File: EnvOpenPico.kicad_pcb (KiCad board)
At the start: 2 copper layers, 21 x 51.3 mm, 26 parts, among them J1 USB_B_Micro, J2 Conn_01x02, J3 Conn_02x18_Odd_Even, J4 Conn_02x18_Odd_Even, J5 Conn_01x03_Male, U1 NCP1117-3.3_SOT223, U2 W25Q16JVSSIQ, U3 RP2040, Y1 ABLS-12.000MHZ-B4-T

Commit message: Redesign
I need sleep.
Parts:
- removed C8: 1u, Capacitor_SMD:C_0402_1005Metric
- added C10: 1u, Capacitor_SMD:C_0402_1005Metric, F.Cu at (94.1, 60.8)
- added C13: 100n, Capacitor_SMD:C_0402_1005Metric, F.Cu at (95.2, 78.5)
- added C14: 100n, Capacitor_SMD:C_0402_1005Metric, F.Cu at (90.4, 83.6)
- added H1: MountingHole, MountingHole:MountingHole_2.7mm_M2.5, F.Cu at (95.7, 50.4)
- added H2: MountingHole, MountingHole:MountingHole_2.7mm_M2.5, F.Cu at (84.4, 98.3)
- added H3: MountingHole, MountingHole:MountingHole_2.7mm_M2.5, F.Cu at (95.8, 98.3)
- added H4: MountingHole, MountingHole:MountingHole_2.7mm_M2.5, F.Cu at (84.4, 50.4)
- C1: footprint Capacitor_SMD:C_0805_2012Metric -> Capacitor_SMD:C_0402_1005Metric
- C4: footprint Capacitor_SMD:C_0805_2012Metric -> Capacitor_SMD:C_0402_1005Metric; moved to F.Cu
- C5, C7, D2, R1, R2: moved to F.Cu
- U2: footprint W25Q16JVSSIQ:SOIC127P790X216-8N -> Package_SO:SOIC-8_5.23x5.23mm_P1.27mm
- moved C6 12.9 mm to (91.4, 83.7), turned to 270 degrees
- moved C4 8.40 mm to (92.9, 59.5), turned to 180 degrees
- moved C5 7.24 mm to (94.0, 69.0), turned to 0 degrees
- moved D3 5.88 mm to (95.7, 75.4)
- moved R8 5.40 mm to (95.2, 76.9), turned to 180 degrees
- moved R5 5.32 mm to (87.9, 91.3), turned to 180 degrees
- moved R2 4.73 mm to (87.8, 60.4), turned to 270 degrees
- moved C7 4.37 mm to (92.6, 71.4)
- moved R1 4.22 mm to (88.9, 60.4)
- moved J2 4.15 mm to (88.1, 58.5)
- moved U1 3.60 mm to (95.4, 56.6)
- moved C2 2.74 mm to (87.9, 87.6), turned to 0 degrees
- moved C3 2.68 mm to (87.4, 89.3), turned to 90 degrees
- moved U2 2.58 mm to (87.0, 67.0), turned to 270 degrees
- moved C1 1.76 mm to (92.4, 56.3), turned to 270 degrees
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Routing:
- net GND: track 70.5 -> 50.0 mm, vias 10 -> 19
- net /QSPI_SD1: track 6.76 -> 19.3 mm
- net /QSPI_SD3: track 15.5 -> 4.19 mm, vias 2 -> 0
- net /QSPI_SD2: track 7.20 -> 17.4 mm
- net /QSPI_SS: track 13.6 -> 23.7 mm, vias 1 -> 0
- net /QSPI_SCLK: track 15.3 -> 5.16 mm, vias 2 -> 0
- net /QSPI_SD0: track 15.2 -> 6.02 mm, vias 2 -> 0
- net /GPIO25: track 7.35 -> 1.16 mm, vias 2 -> 0
- net +3V3: track 53.2 -> 47.1 mm, vias 3 -> 4
- net /GPIO5: track 14.7 -> 20.7 mm, vias 0 -> 1
- net /XOUT: track 5.72 -> 11.4 mm
- net /RUN: track 9.87 -> 14.6 mm
- net Net-(C3-Pad1): track 8.48 -> 4.05 mm
- net +1V1: track 19.6 -> 15.7 mm, vias 3 -> 5
- net /GPIO4: track 16.8 -> 20.4 mm, vias 0 -> 1
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- added copper zone on F.Cu, net +1V1
- added copper zone on F.Cu, net VBUS
- removed copper zone on B.Cu, net +1V1

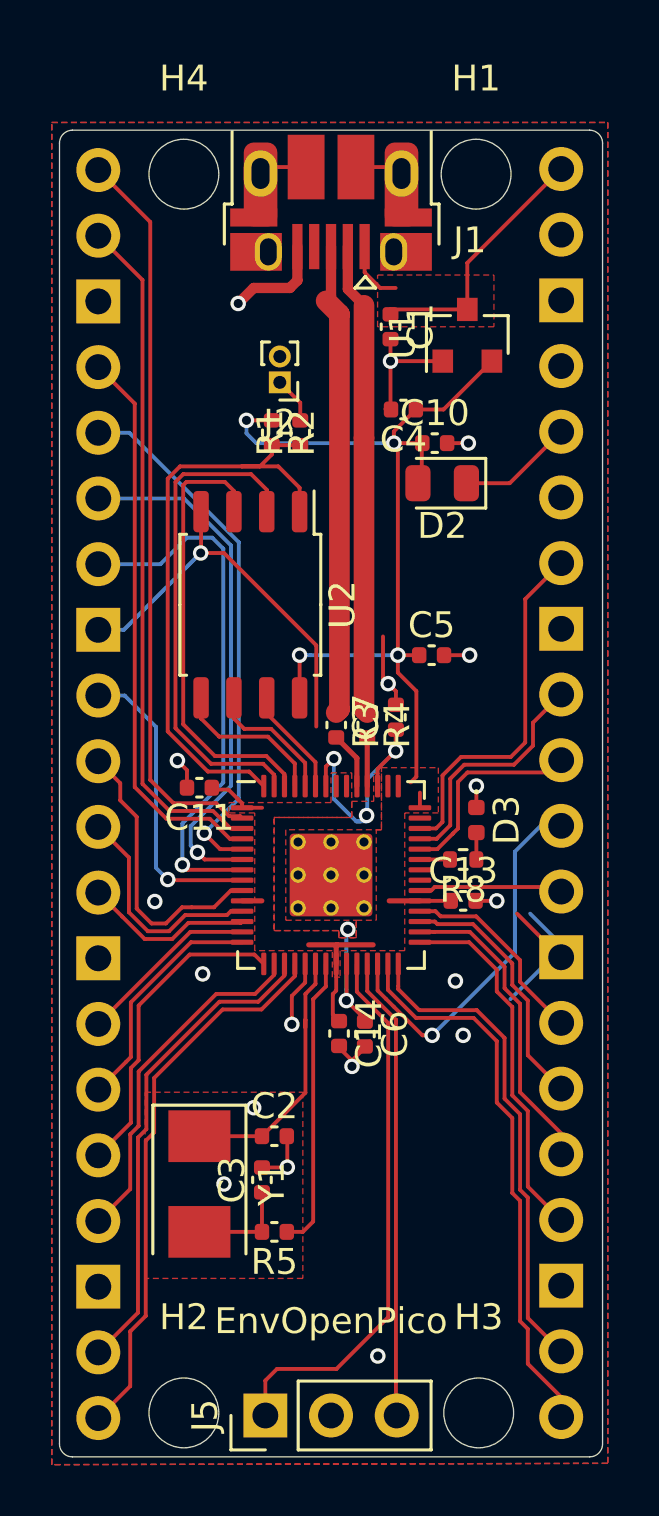
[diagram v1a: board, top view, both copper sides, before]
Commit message: Swapped Crystal for smaller XO oscillator
+ some general other changes
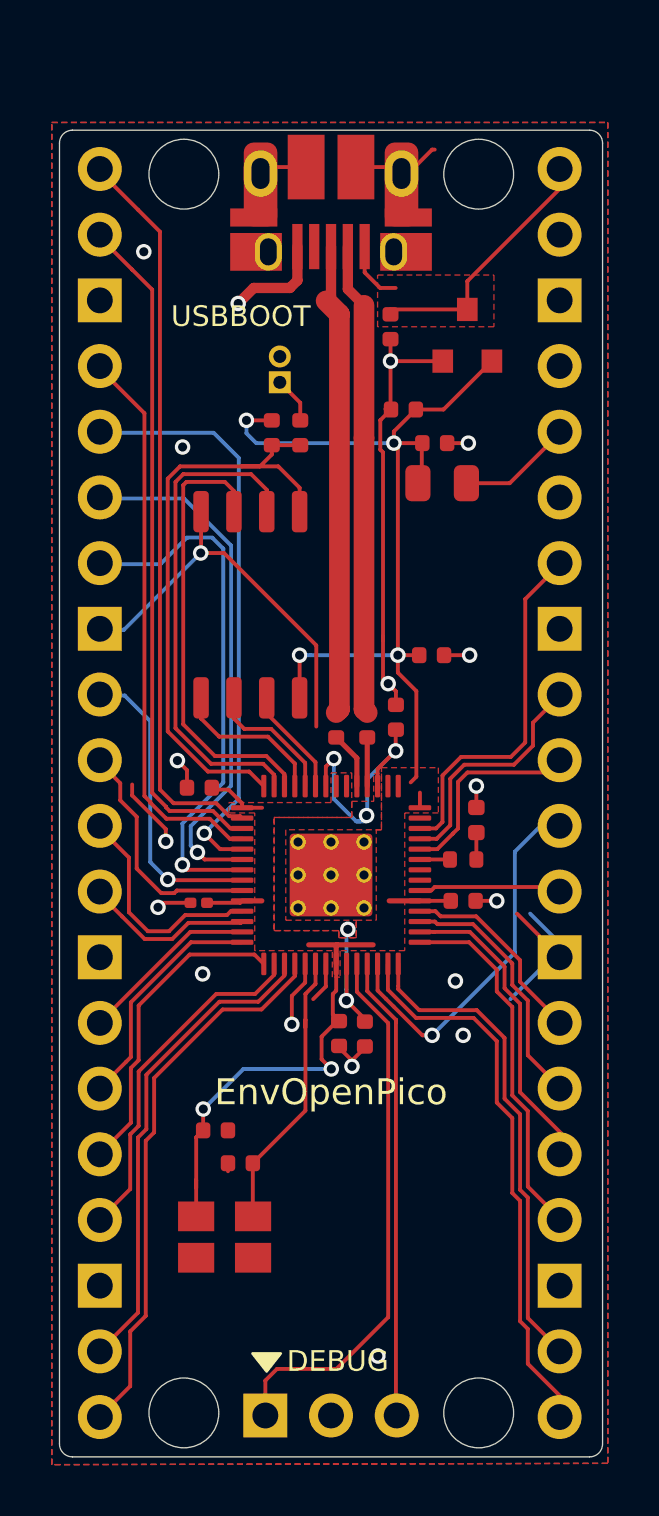
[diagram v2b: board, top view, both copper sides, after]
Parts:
- removed C3: 27p, Capacitor_SMD:C_0402_1005Metric
- removed R5: 1k, Capacitor_SMD:C_0402_1005Metric
- removed Y1: ABLS-12.000MHZ-B4-T, Crystal:Crystal_SMD_5032-2Pin_5.0x3.2mm
- added C15: 100n, Capacitor_SMD:C_0402_1005Metric, F.Cu at (85.6, 87.4)
- added C17: 10u, Capacitor_SMD:C_0201_0603Metric, F.Cu at (85.0, 78.6)
- added X1: XO32, Crystal:Crystal_SMD_SeikoEpson_TSX3225-4Pin_3.2x2.5mm, F.Cu at (86.0, 91.5)
- C2: value 27p -> 15p
- moved C2 1.68 mm to (86.6, 88.6)
- moved H1 0.10 mm to (95.8, 50.4)
- moved J3 0.07 mm to (81.2, 98.5)
- moved J4 0.06 mm to (98.9, 50.2)
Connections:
- C2 pad 1: /XIN -> GND
- C2 pad 2: GND -> /XIN
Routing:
- net +3V3: track 47.1 -> 60.9 mm, vias 4 -> 6
- net GND: track 50.0 -> 62.9 mm
- net /XOUT: track 11.4 -> 1.57 mm
- net Net-(C3-Pad1): track 4.05 -> 0.00 mm
- net /GPIO3: track 20.7 -> 22.6 mm
- net /GPIO7: track 11.2 -> 9.28 mm
- net /XIN: track 10.3 -> 11.1 mm
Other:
- board text added: "3.3V_EN is not implemented"
- board text added: "ADC_VREF is not implemented"
- board text added: "DEBUG"
- board text added: "USBBOOT"
- board text added: "VSYS is not implemented"

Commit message: added more decoupling capacitors+++others
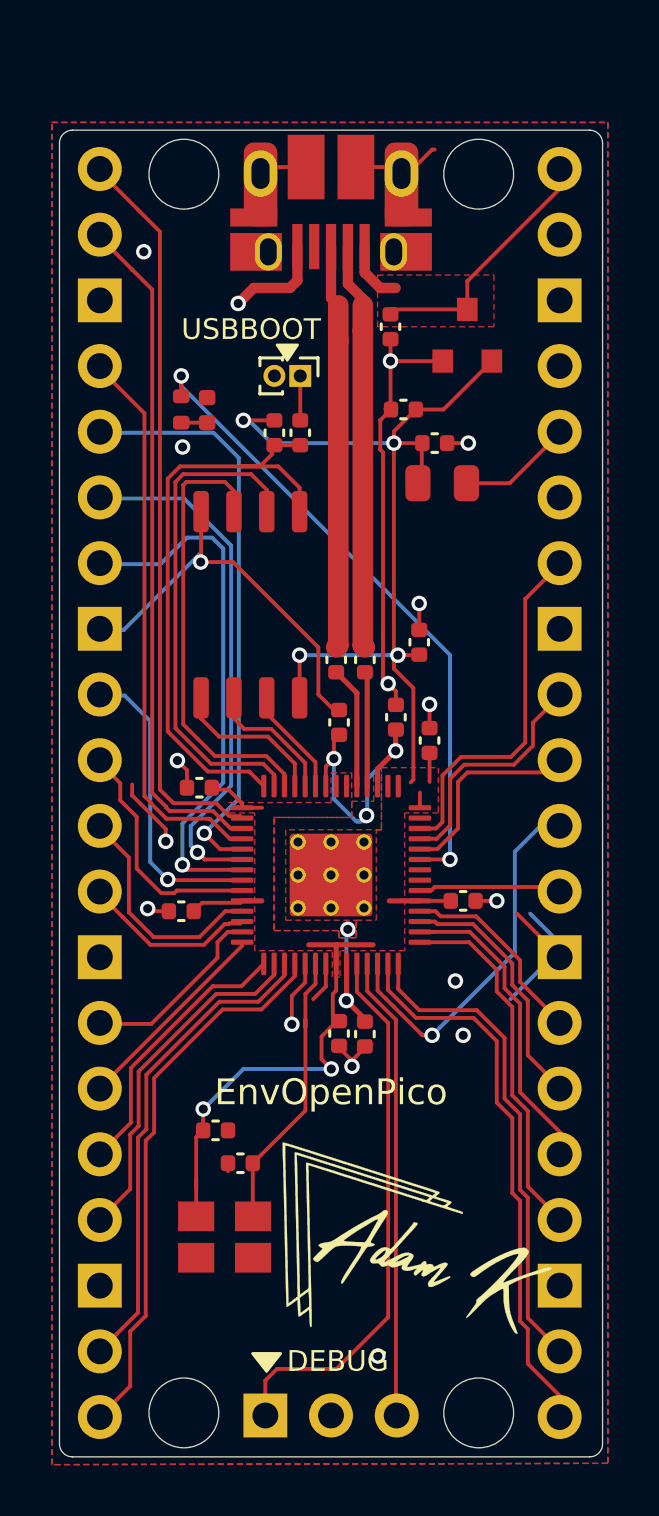
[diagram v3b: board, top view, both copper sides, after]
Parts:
- added C3: 1u, Capacitor_SMD:C_0402_1005Metric, F.Cu at (90.4, 71.6)
- added C8: 100n, Capacitor_SMD:C_0402_1005Metric, F.Cu at (93.9, 72.3)
- added G***: LOGO, EnvExtras:logo, F.Cu at (93.5, 91.7)
- C17: footprint Capacitor_SMD:C_0201_0603Metric -> Capacitor_SMD:C_0402_1005Metric
- moved R8 20.5 mm to (84.3, 59.5), turned to 90 degrees
- moved D3 19.0 mm to (85.3, 59.5)
- moved R4 2.52 mm to (91.4, 69.2)
- moved R3 2.52 mm to (90.3, 69.2)
- moved J2 0.83 mm to (88.9, 58.2), turned to 270 degrees
- moved C17 0.75 mm to (84.3, 78.9)
- moved C5 0.69 mm to (93.5, 68.5), turned to 90 degrees
- moved R2 0.10 mm to (87.9, 60.4)
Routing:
- net /GPIO25: track 1.16 -> 25.0 mm, vias 0 -> 2
- net /USB_D+: track 18.4 -> 15.6 mm
- net Net-(R4-Pad2): track 1.88 -> 4.44 mm
- net /USB_D-: track 18.3 -> 15.8 mm
- net Net-(R3-Pad2): track 2.21 -> 4.73 mm
- net +3V3: track 60.9 -> 62.7 mm
- net /GPIO12: track 12.2 -> 10.7 mm
- net /GPIO11: track 9.16 -> 8.00 mm
- net +1V1: track 15.7 -> 16.7 mm
- net GND: track 62.9 -> 62.4 mm, vias 19 -> 18

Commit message: Replaced MicroB with Type-C
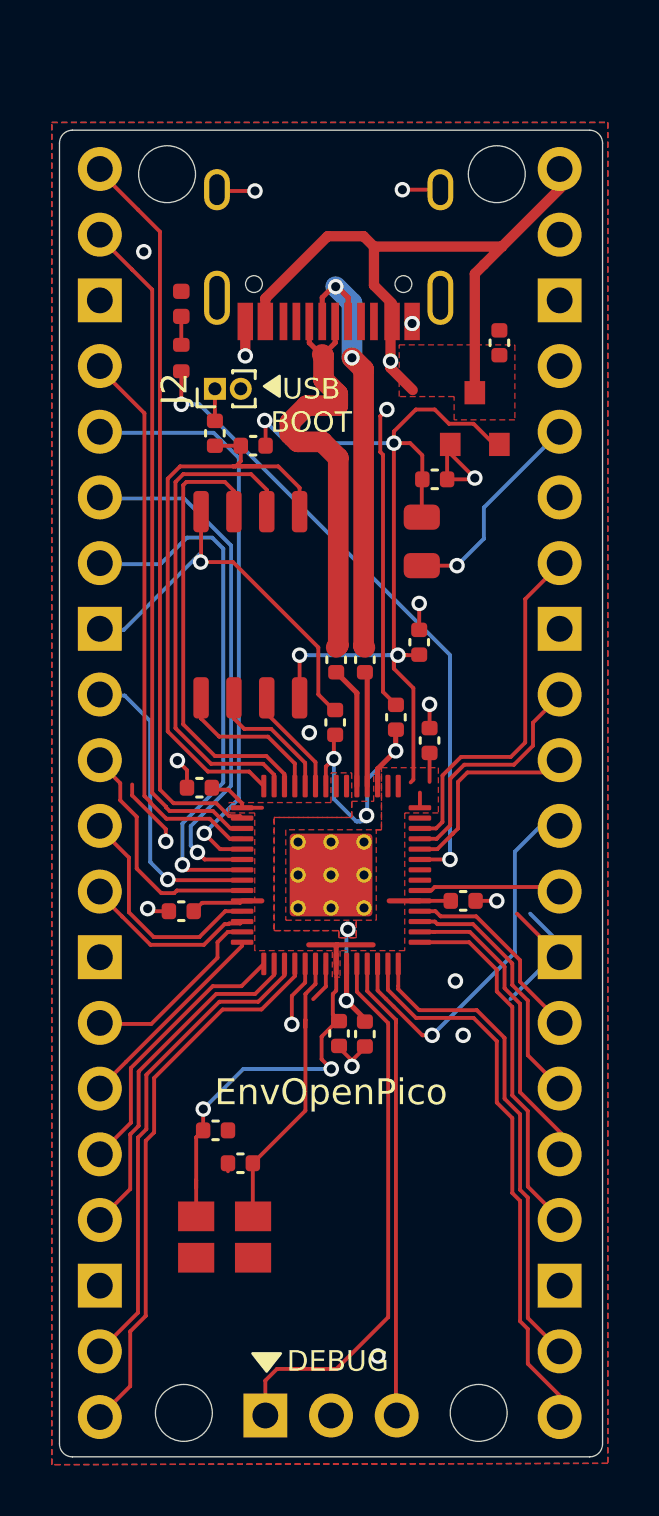
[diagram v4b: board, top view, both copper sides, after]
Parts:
- removed C4: 10u, Capacitor_SMD:C_0402_1005Metric
- removed G***: LOGO, EnvExtras:logo
- removed J1: USB_B_Micro, RP2040_minimal:USB_Micro-B_Amphenol_10103594-0001LF_Horizontal_modified
- added e1: USB_C, HRO-TYPE-C31-M-12:HRO-TYPE-C-31-M-12, F.Cu at (90.0, 48.4)
- H1, H2, H3, H4: footprint MountingHole:MountingHole_2.7mm_M2.5 -> MountingHole:MountingHole_2.2mm_M2
- moved C1 4.26 mm to (96.6, 56.9), turned to 90 degrees
- moved D3 4.23 mm to (84.3, 55.4)
- moved J2 3.34 mm to (85.6, 58.7), turned to 90 degrees
- moved R1 3.30 mm to (85.6, 60.4)
- moved U1 3.23 mm to (95.7, 59.9)
- moved D2 2.38 mm to (93.6, 64.6), turned to 90 degrees
- moved R8 1.99 mm to (84.3, 57.5), turned to 270 degrees
- moved C10 1.40 mm to (94.1, 62.2)
- moved R2 0.96 mm to (87.1, 60.9), turned to 180 degrees
- moved H1 0.70 mm to (96.5, 50.4)
- moved H4 0.65 mm to (83.8, 50.4)
- moved C3 0.15 mm to (90.2, 71.6)
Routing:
- net VBUS: track 12.6 -> 27.2 mm, vias 0 -> 1
- net GND: track 62.4 -> 55.5 mm, vias 18 -> 20
- net Net-(D2-Pad1): track 4.49 -> 8.18 mm, vias 0 -> 1
- net /USB_D-: track 15.8 -> 17.6 mm, vias 0 -> 2
- net /USB_D+: track 15.6 -> 17.3 mm
- net +3V3: track 62.7 -> 63.3 mm
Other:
- board text added: "USB BOOT"
- board text removed: "USBBOOT"

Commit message: I forgot what I went to adjust but I did something or another.
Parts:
- moved C5 2.63 mm to (96.1, 68.9), turned to 180 degrees
- moved R3 2.60 mm to (91.7, 71.4)
- moved R4 2.54 mm to (92.6, 71.4)
- moved C8 2.35 mm to (96.0, 73.3)
- moved D2 2.25 mm to (95.7, 63.7), turned to 0 degrees
- moved C10 2.03 mm to (96.1, 62.1), turned to 180 degrees
- moved C7 1.80 mm to (94.1, 72.3)
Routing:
- net GND: track 55.5 -> 39.1 mm, vias 20 -> 19
- net /USB_D+: track 17.3 -> 20.8 mm, vias 0 -> 1
- net /USB_D-: track 17.6 -> 20.3 mm
- net Net-(R3-Pad2): track 4.73 -> 2.41 mm
- net +1V1: track 16.7 -> 18.4 mm
- net Net-(R4-Pad2): track 4.44 -> 3.06 mm
- net /GPIO25: track 24.8 -> 26.0 mm
- net /GPIO26_ADC0: track 7.94 -> 6.83 mm
- net +3V3: track 63.3 -> 64.4 mm

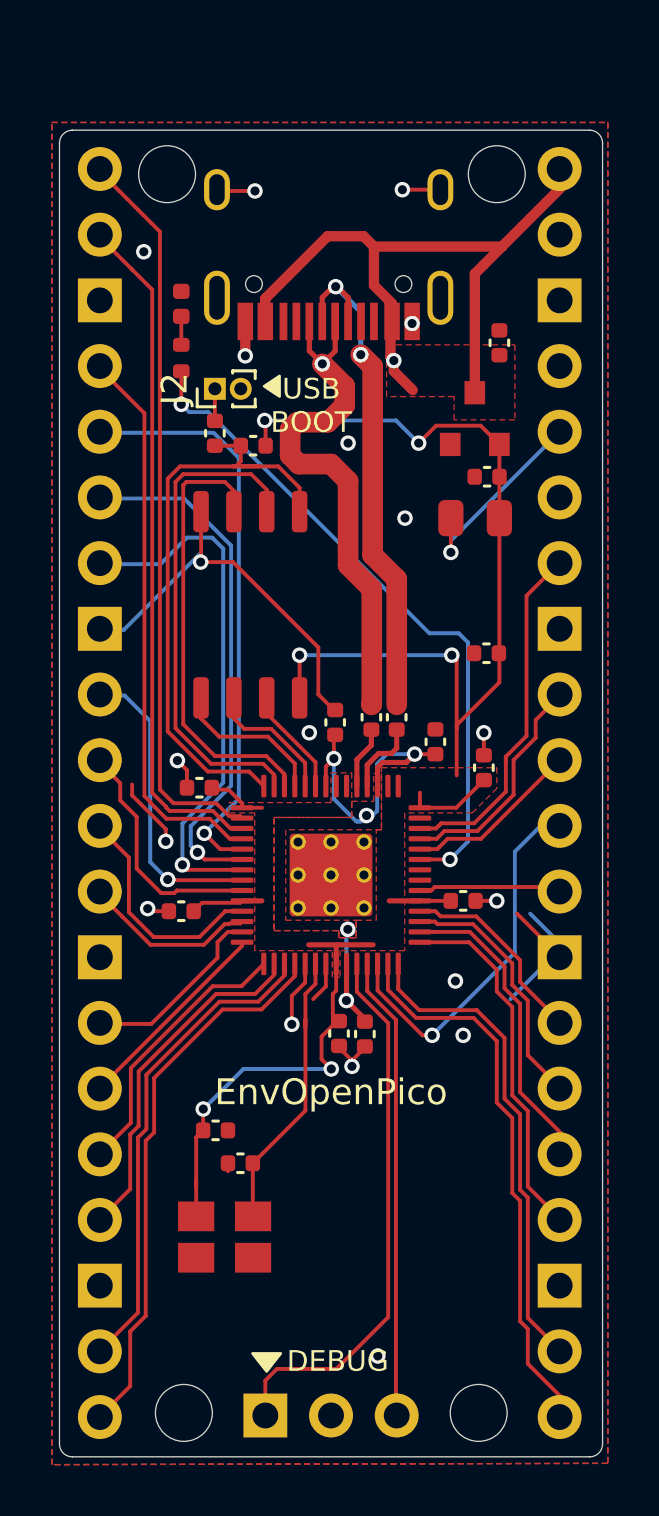
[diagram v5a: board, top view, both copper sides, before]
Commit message: replaced the 3.3V out diode for a smaller one
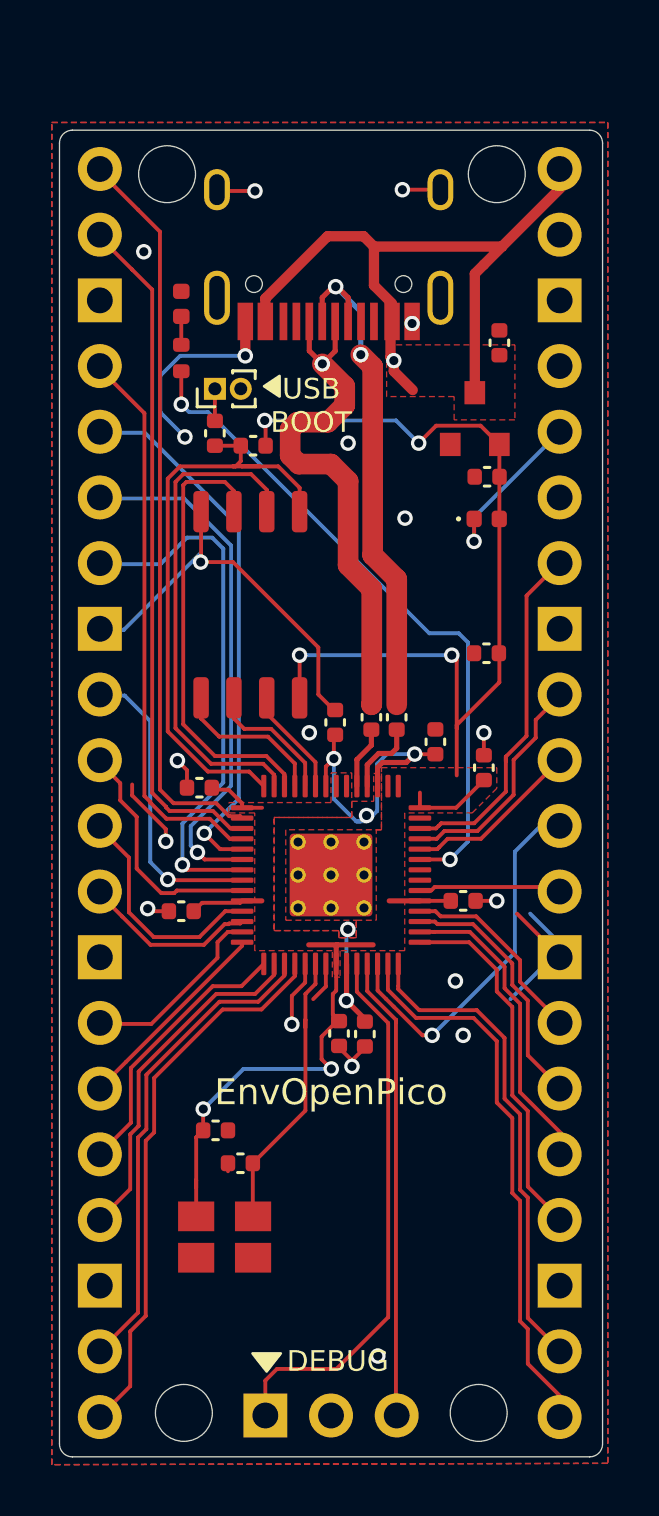
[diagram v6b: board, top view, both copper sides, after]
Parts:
- D2: footprint Diode_SMD:D_0805_2012Metric -> Diode_SMD:D_0402_1005Metric
- moved D2 0.45 mm to (96.1, 63.7)
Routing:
- net GND: track 39.1 -> 45.4 mm, vias 19 -> 20
- net /GPIO3: track 22.6 -> 21.1 mm
- net Net-(D2-Pad1): track 7.73 -> 6.48 mm

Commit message: Made the board 0.09mm wider and adjusted the ground planes
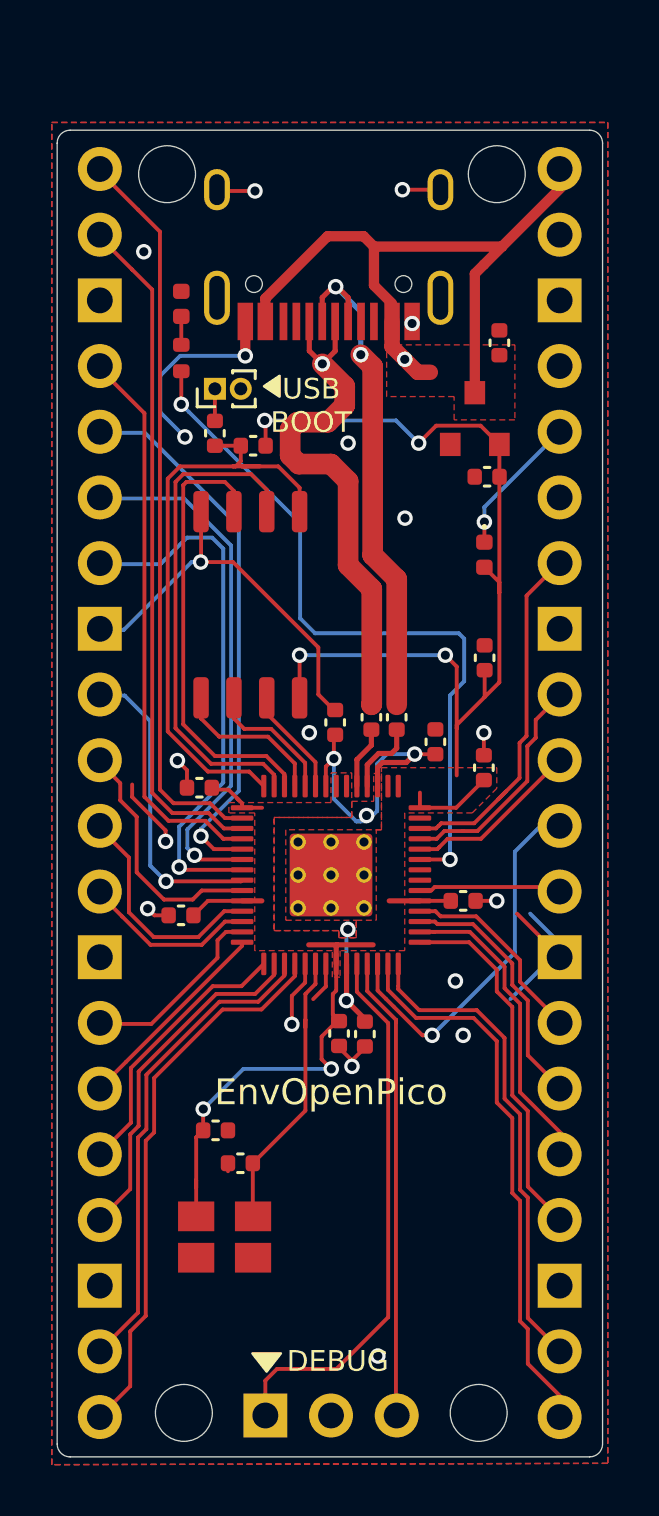
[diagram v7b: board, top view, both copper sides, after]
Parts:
- moved D2 1.39 mm to (96.0, 65.1), turned to 270 degrees
- moved C5 0.19 mm to (96.0, 69.1), turned to 90 degrees
- moved C17 0.16 mm to (84.3, 79.1)
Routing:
- net +3V3: track 64.4 -> 66.5 mm
- net /GPIO25: track 26.0 -> 28.1 mm
- net Net-(D2-Pad1): track 6.48 -> 5.48 mm
- net VBUS: track 27.2 -> 27.8 mm
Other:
- board size 21 x 51.3 mm -> 21.1 x 51.3 mm
